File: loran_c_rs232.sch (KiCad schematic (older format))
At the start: 30 parts

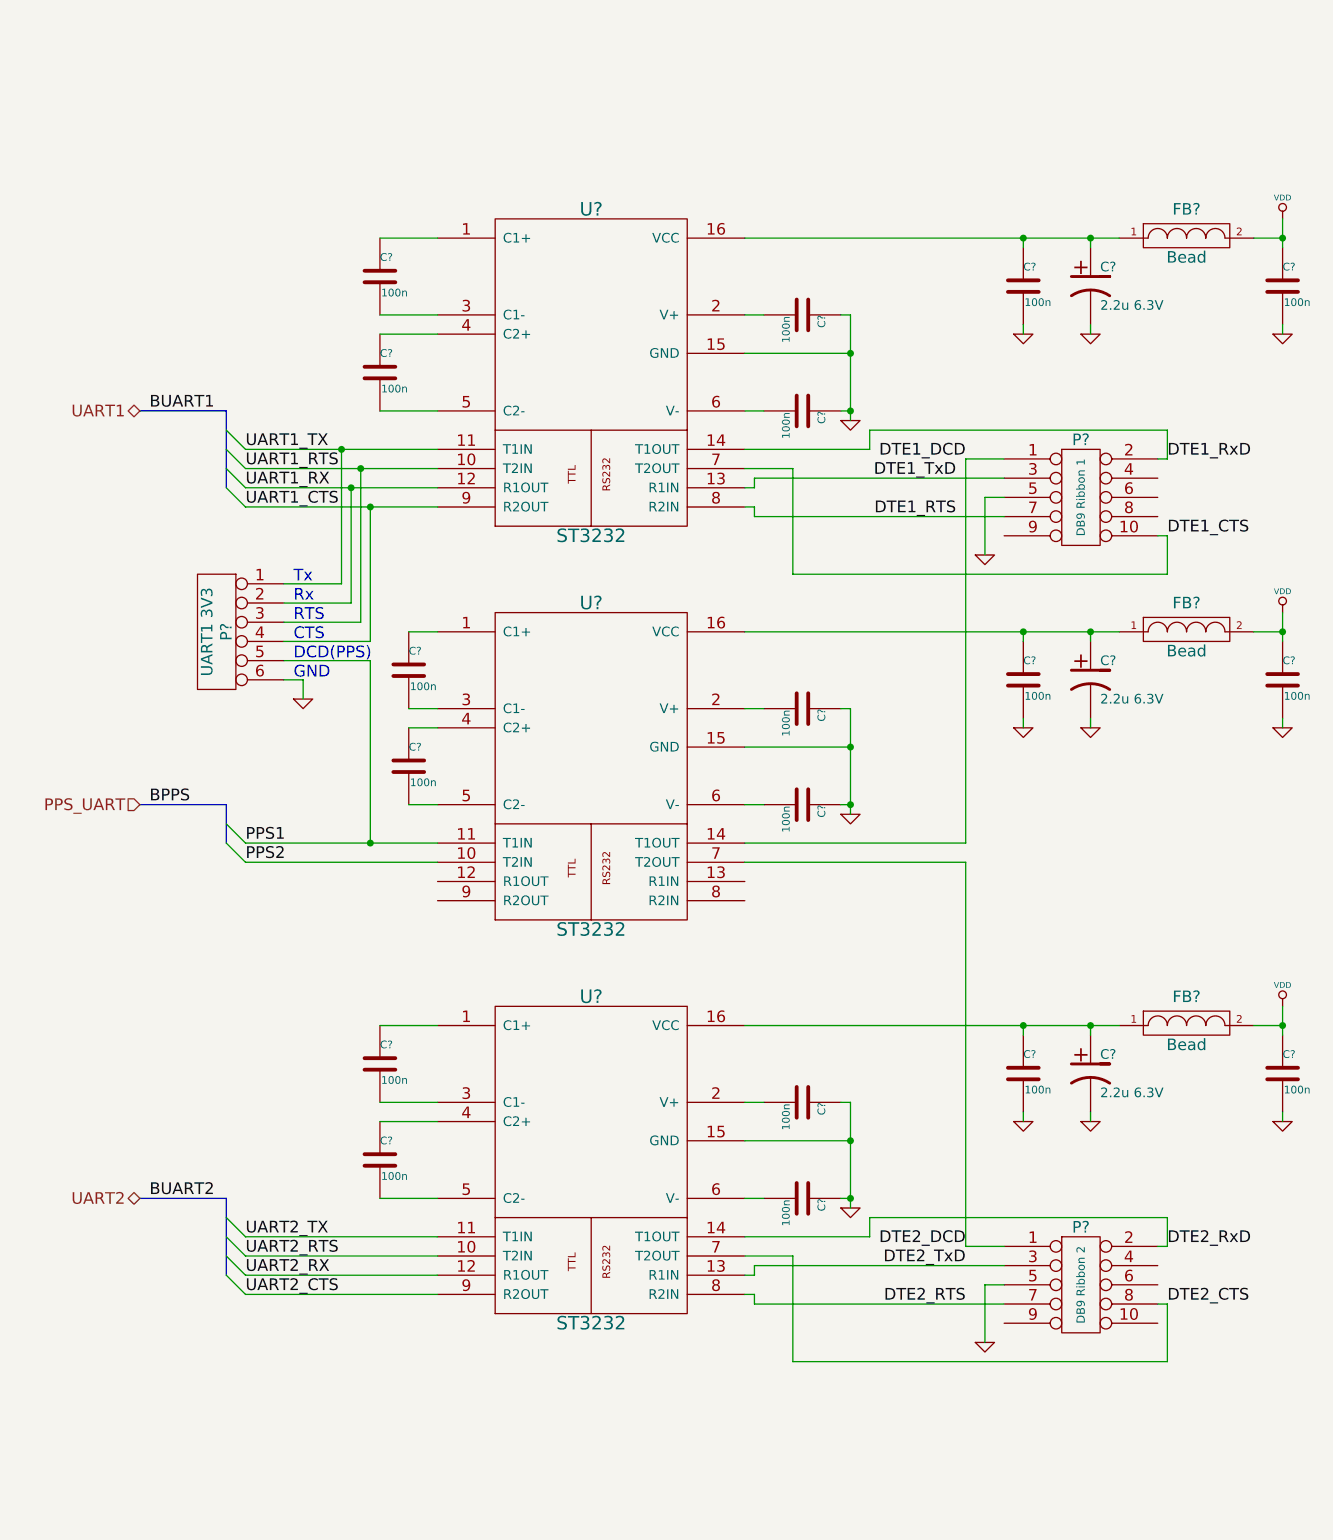
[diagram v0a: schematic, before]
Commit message: Almost done: SPI, Relay optocouplers, ADC & DAC interface However, bug needs to be fixed: buses are not connected between hierarchical sheets
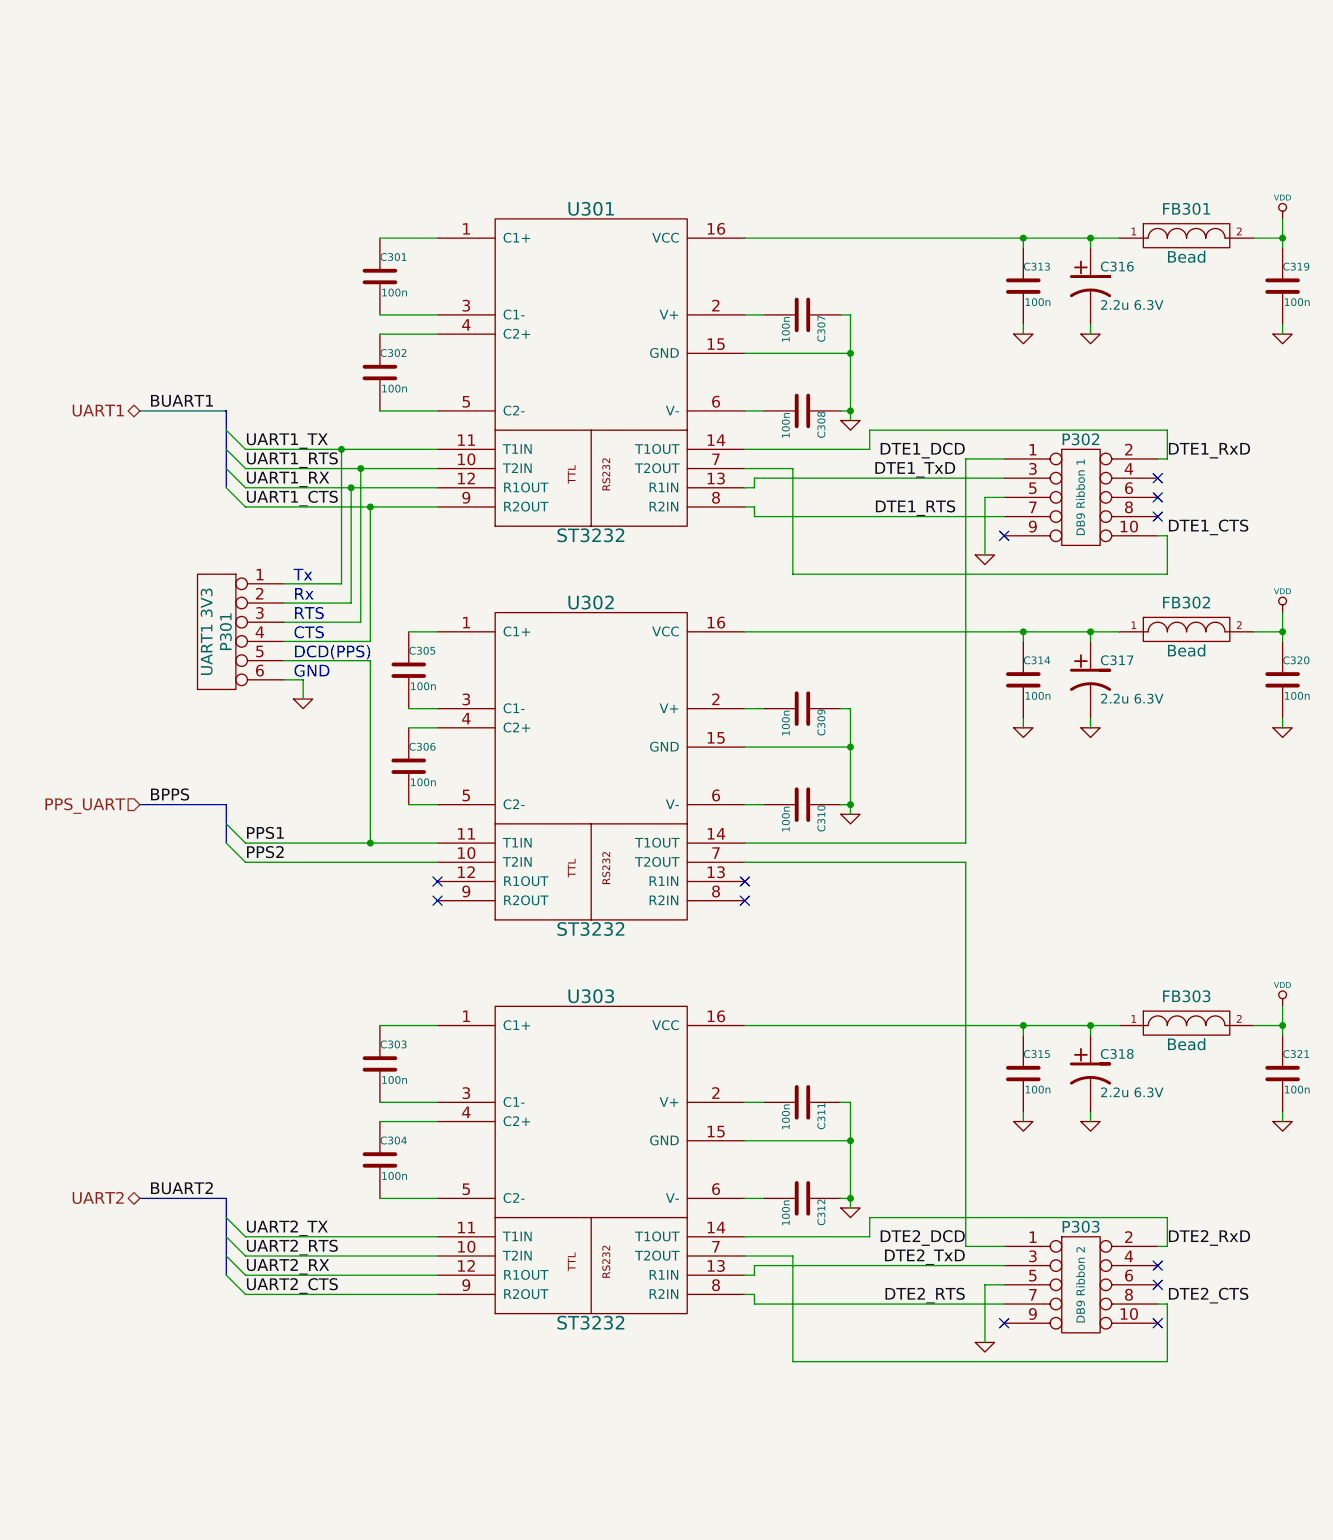
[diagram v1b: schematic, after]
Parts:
- gave numbers to parts that had none: 30
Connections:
- no-connect marks 0 -> 12

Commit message: FIXED: no more buses on hierarchical sheet ports
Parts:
- C316, C317, C318: value 2.2u 6.3V -> 2.2u 6.3V Ta
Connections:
- net PPS1 renamed PPS_UART1
- net PPS2 renamed PPS_UART2
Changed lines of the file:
@@
 $Descr A4 8268 11693 portrait
 encoding utf-8
-Sheet 3 7
+Sheet 2 7
 Title "RS232 level converter"
 Date "18 янв. 2014"
@@
 DTE2_CTS
 $Comp
-L GND #PWR048
+L GND #PWR037
 U 1 1 52DBAE37
 P 5600 7750
-F 0 "#PWR048" H 5600 7750 30  0001 C CNN
+F 0 "#PWR037" H 5600 7750 30  0001 C CNN
 F 1 "GND" H 5600 7680 30  0001 C CNN
 F 2 "" H 5600 7750 60  0000 C CNN
@@
 DTE1_CTS
 $Comp
-L GND #PWR049
+L GND #PWR038
 U 1 1 52DBB093
 P 5600 3650
-F 0 "#PWR049" H 5600 3650 30  0001 C CNN
+F 0 "#PWR038" H 5600 3650 30  0001 C CNN
 F 1 "GND" H 5600 3580 30  0001 C CNN
 F 2 "" H 5600 3650 60  0000 C CNN
@@
 $EndComp
 $Comp
-L GND #PWR050
+L GND #PWR039
 U 1 1 52DBC5A6
 P 4900 2950
-F 0 "#PWR050" H 4900 2950 30  0001 C CNN
+F 0 "#PWR039" H 4900 2950 30  0001 C CNN
 F 1 "GND" H 4900 2880 30  0001 C CNN
 F 2 "" H 4900 2950 60  0000 C CNN
@@
 $EndComp
 $Comp
-L GND #PWR051
+L GND #PWR040
 U 1 1 52DBD4A5
 P 4900 7050
-F 0 "#PWR051" H 4900 7050 30  0001 C CNN
+F 0 "#PWR040" H 4900 7050 30  0001 C CNN
 F 1 "GND" H 4900 6980 30  0001 C CNN
 F 2 "" H 4900 7050 60  0000 C CNN
@@
 $EndComp
 $Comp
-L GND #PWR052
+L GND #PWR041
 U 1 1 52DBD9EF
 P 4900 5000
-F 0 "#PWR052" H 4900 5000 30  0001 C CNN
+F 0 "#PWR041" H 4900 5000 30  0001 C CNN
 F 1 "GND" H 4900 4930 30  0001 C CNN
 F 2 "" H 4900 5000 60  0000 C CNN
@@
 Wire Wire Line
 	5500 7250 5700 7250
-Wire Bus Line
-	1650 2900 1650 3300
-Wire Wire Line
-	1750 3100 2750 3100
-Wire Wire Line
-	1750 3200 2750 3200
-Wire Wire Line
-	1750 3300 2750 3300
-Wire Wire Line
-	1750 3400 2750 3400
-Entry Wire Line
-	1650 3000 1750 3100
-Entry Wire Line
-	1650 3100 1750 3200
-Entry Wire Line
-	1650 3200 1750 3300
-Entry Wire Line
-	1650 3300 1750 3400
+Wire Wire Line
+	1200 3100 2750 3100
+Wire Wire Line
+	1200 3200 2750 3200
+Wire Wire Line
+	1200 3300 2750 3300
+Wire Wire Line
+	1200 3400 2750 3400
 Text Label 1750 3100 0    61   ~ 0
 UART1_TX
@@
 Text Label 1750 3400 0    61   ~ 0
 UART1_CTS
-Wire Bus Line
-	1650 2900 1200 2900
-Text HLabel 1200 2900 0    61   BiDi ~ 0
-UART1
-Text Label 1250 2900 0    61   ~ 0
-BUART1
-Wire Bus Line
-	1650 7000 1650 7400
-Wire Wire Line
-	2750 7200 1750 7200
-Wire Wire Line
-	1750 7300 2750 7300
-Wire Wire Line
-	2750 7400 1750 7400
-Wire Wire Line
-	1750 7500 2750 7500
-Entry Wire Line
-	1650 7100 1750 7200
-Entry Wire Line
-	1650 7200 1750 7300
-Entry Wire Line
-	1650 7300 1750 7400
-Entry Wire Line
-	1650 7400 1750 7500
+Wire Wire Line
+	1200 7200 2750 7200
+Wire Wire Line
+	1200 7300 2750 7300
+Wire Wire Line
+	1200 7400 2750 7400
+Wire Wire Line
+	1200 7500 2750 7500
 Text Label 1750 7200 0    61   ~ 0
 UART2_TX
@@
 Text Label 1750 7500 0    61   ~ 0
 UART2_CTS
-Wire Bus Line
-	1650 7000 1200 7000
-Text HLabel 1200 7000 0    61   BiDi ~ 0
-UART2
-Text Label 1250 7000 0    61   ~ 0
-BUART2
-Wire Bus Line
-	1650 4950 1650 5150
-Wire Wire Line
-	1750 5150 2750 5150
-Entry Wire Line
-	1650 5050 1750 5150
-Entry Wire Line
-	1650 5150 1750 5250
-Text Label 1750 5150 0    61   ~ 0
-PPS1
-Text Label 1750 5250 0    61   ~ 0
-PPS2
-Wire Bus Line
-	1650 4950 1200 4950
-Text HLabel 1200 4950 0    61   Input ~ 0
-PPS_UART
-Text Label 1250 4950 0    61   ~ 0
-BPPS
-Wire Wire Line
-	1750 5250 2750 5250
+Wire Wire Line
+	1200 5150 2750 5150
+Wire Wire Line
+	1200 5250 2750 5250
 $Comp
 L C C313
@@
 P 6150 2250
 F 0 "C316" H 6200 2350 50  0000 L CNN
-F 1 "2.2u 6.3V" H 6200 2150 50  0000 L CNN
+F 1 "2.2u 6.3V Ta" H 6200 2150 50  0000 L CNN
 F 2 "" H 6150 2250 60  0000 C CNN
 F 3 "" H 6150 2250 60  0000 C CNN
@@
 $EndComp
 $Comp
-L GND #PWR053
+L GND #PWR042
 U 1 1 52DC08D0
 P 5800 2500
-F 0 "#PWR053" H 5800 2500 30  0001 C CNN
+F 0 "#PWR042" H 5800 2500 30  0001 C CNN
 F 1 "GND" H 5800 2430 30  0001 C CNN
 F 2 "" H 5800 2500 60  0000 C CNN
@@
 $EndComp
 $Comp
-L GND #PWR054
+L GND #PWR043
 U 1 1 52DC08DB
 P 6150 2500
-F 0 "#PWR054" H 6150 2500 30  0001 C CNN
+F 0 "#PWR043" H 6150 2500 30  0001 C CNN
 F 1 "GND" H 6150 2430 30  0001 C CNN
 F 2 "" H 6150 2500 60  0000 C CNN
@@
 	6150 2000 6150 2050
 Wire Wire Line
-	5800 2050 5800 2000
+	5800 1950 5800 2050
 Connection ~ 5800 2000
 Wire Wire Line
@@
 $EndComp
 $Comp
-L GND #PWR055
+L GND #PWR044
 U 1 1 52DC0F53
 P 7150 2500
-F 0 "#PWR055" H 7150 2500 30  0001 C CNN
+F 0 "#PWR044" H 7150 2500 30  0001 C CNN
 F 1 "GND" H 7150 2430 30  0001 C CNN
 F 2 "" H 7150 2500 60  0000 C CNN
@@
 Connection ~ 7150 2000
 $Comp
-L VDD #PWR056
+L VDD #PWR045
 U 1 1 52DC1066
 P 7150 1900
-F 0 "#PWR056" H 7150 2000 30  0001 C CNN
+F 0 "#PWR045" H 7150 2000 30  0001 C CNN
 F 1 "VDD" H 7150 2010 30  0000 C CNN
 F 2 "" H 7150 1900 60  0000 C CNN
@@
 P 6150 4300
 F 0 "C317" H 6200 4400 50  0000 L CNN
-F 1 "2.2u 6.3V" H 6200 4200 50  0000 L CNN
+F 1 "2.2u 6.3V Ta" H 6200 4200 50  0000 L CNN
 F 2 "" H 6150 4300 60  0000 C CNN
 F 3 "" H 6150 4300 60  0000 C CNN
@@
 $EndComp
 $Comp
-L GND #PWR057
+L GND #PWR046
 U 1 1 52DC12C1
 P 5800 4550
-F 0 "#PWR057" H 5800 4550 30  0001 C CNN
+F 0 "#PWR046" H 5800 4550 30  0001 C CNN
 F 1 "GND" H 5800 4480 30  0001 C CNN
 F 2 "" H 5800 4550 60  0000 C CNN
@@
 $EndComp
 $Comp
-L GND #PWR058
+L GND #PWR047
 U 1 1 52DC12C7
 P 6150 4550
-F 0 "#PWR058" H 6150 4550 30  0001 C CNN
+F 0 "#PWR047" H 6150 4550 30  0001 C CNN
 F 1 "GND" H 6150 4480 30  0001 C CNN
 F 2 "" H 6150 4550 60  0000 C CNN
@@
 	6150 4050 6150 4100
 Wire Wire Line
-	5800 4100 5800 4050
+	5800 4000 5800 4100
 Connection ~ 5800 4050
 Wire Wire Line
@@
 $EndComp
 $Comp
-L GND #PWR059
+L GND #PWR048
 U 1 1 52DC12DF
 P 7150 4550
-F 0 "#PWR059" H 7150 4550 30  0001 C CNN
+F 0 "#PWR048" H 7150 4550 30  0001 C CNN
 F 1 "GND" H 7150 4480 30  0001 C CNN
 F 2 "" H 7150 4550 60  0000 C CNN
@@
 Connection ~ 7150 4050
 $Comp
-L VDD #PWR060
+L VDD #PWR049
 U 1 1 52DC12EA
 P 7150 3950
-F 0 "#PWR060" H 7150 4050 30  0001 C CNN
+F 0 "#PWR049" H 7150 4050 30  0001 C CNN
 F 1 "VDD" H 7150 4060 30  0000 C CNN
 F 2 "" H 7150 3950 60  0000 C CNN
@@
 P 6150 6350
 F 0 "C318" H 6200 6450 50  0000 L CNN
-F 1 "2.2u 6.3V" H 6200 6250 50  0000 L CNN
+F 1 "2.2u 6.3V Ta" H 6200 6250 50  0000 L CNN
 F 2 "" H 6150 6350 60  0000 C CNN
 F 3 "" H 6150 6350 60  0000 C CNN
@@
 $EndComp
 $Comp
-L GND #PWR061
+L GND #PWR050
 U 1 1 52DC12FF
 P 5800 6600
-F 0 "#PWR061" H 5800 6600 30  0001 C CNN
+F 0 "#PWR050" H 5800 6600 30  0001 C CNN
 F 1 "GND" H 5800 6530 30  0001 C CNN
 F 2 "" H 5800 6600 60  0000 C CNN
@@
 $EndComp
 $Comp
-L GND #PWR062
+L GND #PWR051
 U 1 1 52DC1305
 P 6150 6600
-F 0 "#PWR062" H 6150 6600 30  0001 C CNN
+F 0 "#PWR051" H 6150 6600 30  0001 C CNN
 F 1 "GND" H 6150 6530 30  0001 C CNN
 F 2 "" H 6150 6600 60  0000 C CNN
@@
 	6150 6100 6150 6150
 Wire Wire Line
-	5800 6150 5800 6100
+	5800 6050 5800 6150
 Connection ~ 5800 6100
 Wire Wire Line
@@
 $EndComp
 $Comp
-L GND #PWR063
+L GND #PWR052
 U 1 1 52DC131D
 P 7150 6600
-F 0 "#PWR063" H 7150 6600 30  0001 C CNN
+F 0 "#PWR052" H 7150 6600 30  0001 C CNN
 F 1 "GND" H 7150 6530 30  0001 C CNN
 F 2 "" H 7150 6600 60  0000 C CNN
@@
 Connection ~ 7150 6100
 $Comp
-L VDD #PWR064
+L VDD #PWR053
 U 1 1 52DC1328
 P 7150 6000
-F 0 "#PWR064" H 7150 6100 30  0001 C CNN
+F 0 "#PWR053" H 7150 6100 30  0001 C CNN
 F 1 "VDD" H 7150 6110 30  0000 C CNN
 F 2 "" H 7150 6000 60  0000 C CNN
@@
 	2050 4300 2050 4400
 $Comp
-L GND #PWR065
+L GND #PWR054
 U 1 1 52DC2978
 P 2050 4400
-F 0 "#PWR065" H 2050 4400 30  0001 C CNN
+F 0 "#PWR054" H 2050 4400 30  0001 C CNN
 F 1 "GND" H 2050 4330 30  0001 C CNN
 F 2 "" H 2050 4400 60  0000 C CNN
@@
 NoConn ~ 6500 3450
 NoConn ~ 5700 3550
+Text HLabel 1200 3100 0    61   Input ~ 0
+UART1_TX
+Text HLabel 1200 3200 0    61   Input ~ 0
+UART1_RTS
+Text HLabel 1200 3300 0    61   Output ~ 0
+UART1_RX
+Text HLabel 1200 3400 0    61   Output ~ 0
+UART1_CTS
+Text HLabel 1200 5150 0    61   Input ~ 0
+PPS_UART1
+Text HLabel 1200 5250 0    61   Input ~ 0
+PPS_UART2
+Text HLabel 1200 7200 0    61   Input ~ 0
+UART2_TX
+Text HLabel 1200 7300 0    61   Input ~ 0
+UART2_RTS
+Text HLabel 1200 7400 0    61   Output ~ 0
+UART2_RX
+Text HLabel 1200 7500 0    61   Output ~ 0
+UART2_CTS
+$Comp
+L PWR_FLAG #FLG055
+U 1 1 52E7FFCD
+P 5800 1950
+F 0 "#FLG055" H 5800 2045 30  0001 C CNN
+F 1 "PWR_FLAG" H 5800 2130 30  0000 C CNN
+F 2 "" H 5800 1950 60  0000 C CNN
+F 3 "" H 5800 1950 60  0000 C CNN
+	1    5800 1950
+	1    0    0    -1
+$EndComp
+$Comp
+L PWR_FLAG #FLG056
+U 1 1 52E80075
+P 5800 4000
+F 0 "#FLG056" H 5800 4095 30  0001 C CNN
+F 1 "PWR_FLAG" H 5800 4180 30  0000 C CNN
+F 2 "" H 5800 4000 60  0000 C CNN
+F 3 "" H 5800 4000 60  0000 C CNN
+	1    5800 4000
+	1    0    0    -1
+$EndComp
+$Comp
+L PWR_FLAG #FLG057
+U 1 1 52E8010C
+P 5800 6050
+F 0 "#FLG057" H 5800 6145 30  0001 C CNN
+F 1 "PWR_FLAG" H 5800 6230 30  0000 C CNN
+F 2 "" H 5800 6050 60  0000 C CNN
+F 3 "" H 5800 6050 60  0000 C CNN
+	1    5800 6050
+	1    0    0    -1
+$EndComp
 $EndSCHEMATC
